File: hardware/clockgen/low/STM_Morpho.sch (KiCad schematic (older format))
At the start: 13 parts, among them CN10 Conn_02x19_Odd_Even, CN7 Conn_02x19_Odd_Even, J1 Conn_02x20_Odd_Even, U1 74ALVC164245DLG4, U2 74ALVC164245DLG4

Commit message: Two PCBs are routed
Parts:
- J1: symbol Connector_Generic:Conn_02x20_Counter_Clockwise -> Connector_Generic:Conn_02x20_Odd_Even
- U1, U2: symbol 2021-08-26_08-32-07:74ALVC164245DLG4 -> STM_Morpho-rescue:74ALVC164245DLG4-2021-08-26_08-32-07
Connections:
- net +3V3: now also J1.3 (Pin_3); no longer J1.2 (Pin_2)
- net GND: now also J1.2 (Pin_2), J1.38 (Pin_38), J1.4 (Pin_4); no longer J1.21 (Pin_21), J1.22 (Pin_22), J1.39 (Pin_39)
- net NC: now also J1.37 (Pin_37), J1.39 (Pin_39); no longer J1.19 (Pin_19), J1.20 (Pin_20)
- net PA0_5V: now also J1.27 (Pin_27); no longer J1.7 (Pin_7)
- net PA10_5V: now also J1.35 (Pin_35); no longer J1.3 (Pin_3)
- net PA11_5V: now also J1.34 (Pin_34); no longer J1.24 (Pin_24)
- net PA12_5V: now also J1.32 (Pin_32); no longer J1.25 (Pin_25)
- net PA13_5V: now also J1.30 (Pin_30); no longer J1.26 (Pin_26)
- net PA14_5V: now also J1.28 (Pin_28); no longer J1.27 (Pin_27)
- net PA15_5V: now also J1.26 (Pin_26); no longer J1.28 (Pin_28)
- net PA1_5V: now also J1.15 (Pin_15); no longer J1.13 (Pin_13)
- net PA2_5V: now also J1.13 (Pin_13); no longer J1.14 (Pin_14)
- net PA3_5V: now also J1.11 (Pin_11); no longer J1.15 (Pin_15)
- net PA4_5V: now also J1.9 (Pin_9); no longer J1.16 (Pin_16)
- net PA5_5V: now also J1.7 (Pin_7); no longer J1.17 (Pin_17)
- net PA6_5V: now also J1.19 (Pin_19); no longer J1.11 (Pin_11)
- net PA7_5V: now also J1.17 (Pin_17); no longer J1.12 (Pin_12)
- net PA8_5V: now also J1.5 (Pin_5); no longer J1.18 (Pin_18)
- net PA9_5V: now also J1.36 (Pin_36); no longer J1.23 (Pin_23)
- net PB10_5V: now also J1.33 (Pin_33); no longer J1.4 (Pin_4)
- net PB5_5V: now also J1.31 (Pin_31); no longer J1.5 (Pin_5)
- net PB6_5V: now also J1.29 (Pin_29); no longer J1.6 (Pin_6)
- net PB8_5V: now also J1.23 (Pin_23); no longer J1.9 (Pin_9)
- net PB9_5V: now also J1.21 (Pin_21); no longer J1.10 (Pin_10)
- net PC0_5V: now also J1.24 (Pin_24); no longer J1.29 (Pin_29)
- net PC10_5V: now also J1.6 (Pin_6); no longer J1.38 (Pin_38)
- net PC1_5V: now also J1.22 (Pin_22); no longer J1.30 (Pin_30)
- net PC2_5V: now also J1.20 (Pin_20); no longer J1.31 (Pin_31)
- net PC3_5V: now also J1.18 (Pin_18); no longer J1.32 (Pin_32)
- net PC4_5V: now also J1.16 (Pin_16); no longer J1.33 (Pin_33)
- net PC5_5V: now also J1.14 (Pin_14); no longer J1.34 (Pin_34)
- net PC6_5V: now also J1.12 (Pin_12); no longer J1.35 (Pin_35)
- net PC7_5V: now also J1.25 (Pin_25); no longer J1.8 (Pin_8)
- net PC8_5V: now also J1.10 (Pin_10); no longer J1.36 (Pin_36)
- net PC9_5V: now also J1.8 (Pin_8); no longer J1.37 (Pin_37)
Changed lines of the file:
@@
 PA3
 $Comp
-L 2021-08-26_08-32-07:74ALVC164245DLG4 U1
+L STM_Morpho-rescue:74ALVC164245DLG4-2021-08-26_08-32-07 U1
 U 1 1 6128B1C2
 P 4400 1050
@@
 PULLUP
 $Comp
-L 2021-08-26_08-32-07:74ALVC164245DLG4 U2
+L STM_Morpho-rescue:74ALVC164245DLG4-2021-08-26_08-32-07 U2
 U 1 1 6130056B
 P 8750 1050
@@
 Text Label 13300 2600 0    50   ~ 0
 PA9_5V
-Text Label 12800 2600 2    50   ~ 0
-PA8_5V
-Text Label 12800 2500 2    50   ~ 0
-PA5_5V
-Text Label 12800 2400 2    50   ~ 0
-PA4_5V
-Text Label 12800 2300 2    50   ~ 0
-PA3_5V
-Text Label 12800 2200 2    50   ~ 0
-PA2_5V
-Text Label 12800 2100 2    50   ~ 0
-PA1_5V
-$Comp
-L Connector_Generic:Conn_02x20_Counter_Clockwise J1
-U 1 1 612BBAFC
-P 13000 1800
-F 0 "J1" H 13050 2917 50  0000 C CNN
-F 1 "Conn_02x20_Odd_Even" H 13050 2826 50  0000 C CNN
-F 2 "Connector_PinHeader_2.54mm:PinHeader_2x20_P2.54mm_Vertical" H 13000 1800 50  0001 C CNN
-F 3 "~" H 13000 1800 50  0001 C CNN
-	1    13000 1800
-	1    0    0    -1
-$EndComp
 $Comp
 L power:GND #PWR06
@@
 	1    0    0    -1
 $EndComp
-Text Label 12800 2000 2    50   ~ 0
-PA7_5V
-Text Label 12800 1900 2    50   ~ 0
-PA6_5V
-Text Label 12800 1800 2    50   ~ 0
-PB9_5V
-Text Label 12800 1700 2    50   ~ 0
-PB8_5V
-Text Label 12800 1600 2    50   ~ 0
-PC7_5V
-Text Label 12800 1500 2    50   ~ 0
-PA0_5V
-Text Label 12800 1400 2    50   ~ 0
-PB6_5V
-Text Label 12800 1300 2    50   ~ 0
-PB5_5V
-Text Label 12800 1200 2    50   ~ 0
-PB10_5V
-Text Label 12800 1100 2    50   ~ 0
-PA10_5V
 Text Label 14400 2850 2    50   ~ 0
 PULLUP
+$Comp
+L Connector_Generic:Conn_02x20_Odd_Even J1
+U 1 1 612BBAFC
+P 13000 1800
+F 0 "J1" H 13050 2917 50  0000 C CNN
+F 1 "Conn_02x20_Odd_Even" H 13050 2826 50  0000 C CNN
+F 2 "Connector_PinHeader_2.54mm:PinHeader_2x20_P2.54mm_Vertical" H 13000 1800 50  0001 C CNN
+F 3 "~" H 13000 1800 50  0001 C CNN
+	1    13000 1800
+	1    0    0    -1
+$EndComp
+Connection ~ 14400 2550
+Text Label 12800 2600 2    50   ~ 0
+PA10_5V
+Text Label 12800 2500 2    50   ~ 0
+PB10_5V
+Text Label 12800 2400 2    50   ~ 0
+PB5_5V
+Text Label 12800 2300 2    50   ~ 0
+PB6_5V
+Text Label 12800 2200 2    50   ~ 0
+PA0_5V
+Text Label 12800 2100 2    50   ~ 0
+PC7_5V
+Text Label 12800 2000 2    50   ~ 0
+PB8_5V
+Text Label 12800 1900 2    50   ~ 0
+PB9_5V
+Text Label 12800 1800 2    50   ~ 0
+PA6_5V
+Text Label 12800 1700 2    50   ~ 0
+PA7_5V
+Text Label 12800 1600 2    50   ~ 0
+PA1_5V
+Text Label 12800 1500 2    50   ~ 0
+PA2_5V
+Text Label 12800 1400 2    50   ~ 0
+PA3_5V
+Text Label 12800 1300 2    50   ~ 0
+PA4_5V
+Text Label 12800 1200 2    50   ~ 0
+PA5_5V
+Text Label 12800 1100 2    50   ~ 0
+PA8_5V
 $EndSCHEMATC

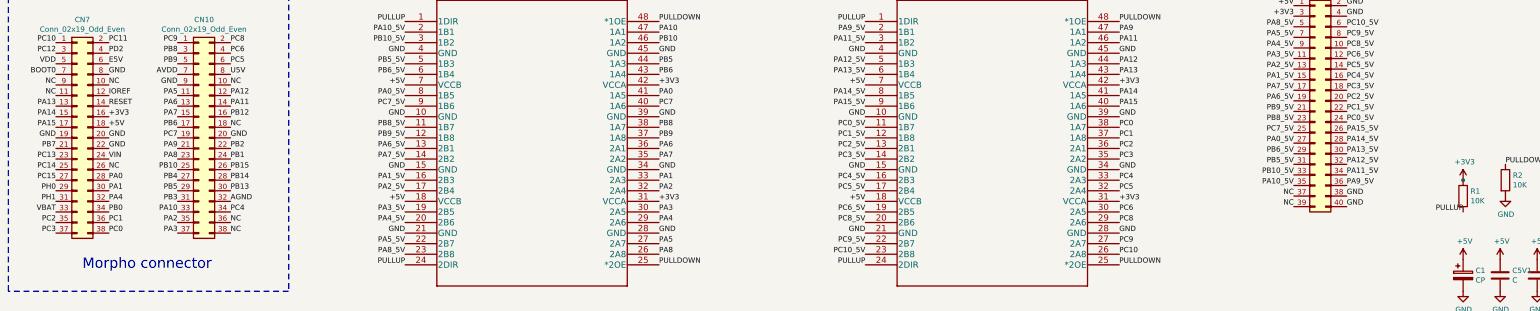
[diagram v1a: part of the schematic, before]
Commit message: Screw terminal adapter added
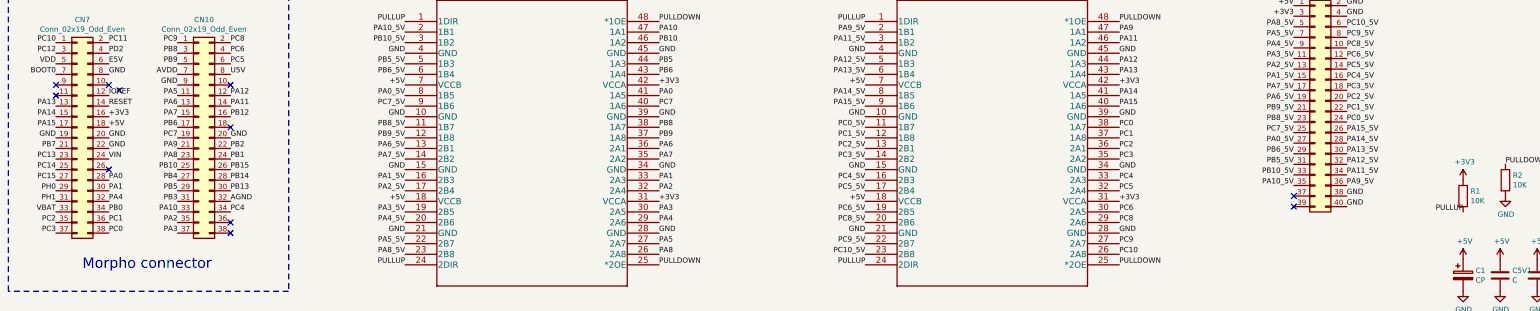
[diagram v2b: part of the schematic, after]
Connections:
- removed net NC: CN10.10 (Pin_10), CN10.18 (Pin_18), CN10.36 (Pin_36), CN10.38 (Pin_38), CN7.10 (Pin_10), CN7.11 (Pin_11), CN7.26 (Pin_26), CN7.9 (Pin_9), J1.37 (Pin_37), J1.39 (Pin_39)
- no-connect marks 0 -> 11
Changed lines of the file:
@@
 $EndDescr
-$Comp
-L Connector_Generic:Conn_02x19_Odd_Even CN7
-U 1 1 5F9F2DD0
-P 1300 2150
-F 0 "CN7" H 1350 3267 50  0000 C CNN
-F 1 "Conn_02x19_Odd_Even" H 1350 3176 50  0000 C CNN
-F 2 "Connector_PinSocket_2.54mm:PinSocket_2x19_P2.54mm_Vertical" H 1300 2150 50  0001 C CNN
-F 3 "~" H 1300 2150 50  0001 C CNN
-	1    1300 2150
-	1    0    0    -1
-$EndComp
 $Comp
 L Connector_Generic:Conn_02x19_Odd_Even CN10
@@
 Text Label 1100 1550 2    50   ~ 0
 BOOT0
-Text Label 1100 1650 2    50   ~ 0
-NC
-Text Label 1100 1750 2    50   ~ 0
-NC
 Text Label 1100 1850 2    50   ~ 0
 PA13
@@
 Text Label 1600 1550 0    50   ~ 0
 GND
-Text Label 1600 1650 0    50   ~ 0
-NC
 Text Label 1600 1750 0    50   ~ 0
 IOREF
@@
 Text Label 1600 2350 0    50   ~ 0
 VIN
-Text Label 1600 2450 0    50   ~ 0
-NC
 Text Label 1600 2550 0    50   ~ 0
 PA0
@@
 Text Label 2750 1550 0    50   ~ 0
 U5V
-Text Label 2750 1650 0    50   ~ 0
-NC
 Text Label 2750 1750 0    50   ~ 0
 PA12
@@
 Text Label 2750 1950 0    50   ~ 0
 PB12
-Text Label 2750 2050 0    50   ~ 0
-NC
 Text Label 2750 2150 0    50   ~ 0
 GND
@@
 Text Label 2750 2850 0    50   ~ 0
 PC4
-Text Label 2750 2950 0    50   ~ 0
-NC
-Text Label 2750 3050 0    50   ~ 0
-NC
 Text Label 2250 1250 2    50   ~ 0
 PC9
@@
 Text Label 15300 7750 1    50   ~ 0
 GND
-Text Label 12800 2800 2    50   ~ 0
-NC
-Text Label 12800 2700 2    50   ~ 0
-NC
 Text Label 13300 2800 0    50   ~ 0
 GND
@@
 	1    0    0    -1
 $EndComp
-Connection ~ 14400 2550
 Text Label 12800 2600 2    50   ~ 0
 PA10_5V
@@
 Text Label 12800 1100 2    50   ~ 0
 PA8_5V
+NoConn ~ 12800 2800
+NoConn ~ 12800 2700
+NoConn ~ 2750 2950
+NoConn ~ 2750 3050
+$Comp
+L Connector_Generic:Conn_02x19_Odd_Even CN7
+U 1 1 5F9F2DD0
+P 1300 2150
+F 0 "CN7" H 1350 3267 50  0000 C CNN
+F 1 "Conn_02x19_Odd_Even" H 1350 3176 50  0000 C CNN
+F 2 "Connector_PinSocket_2.54mm:PinSocket_2x19_P2.54mm_Vertical" H 1300 2150 50  0001 C CNN
+F 3 "~" H 1300 2150 50  0001 C CNN
+	1    1300 2150
+	1    0    0    -1
+$EndComp
+NoConn ~ 1600 2450
+NoConn ~ 1100 1650
+NoConn ~ 1100 1750
+NoConn ~ 2750 1650
+NoConn ~ 2750 2050
+NoConn ~ 1600 1650
+NoConn ~ 1700 1700
 $EndSCHEMATC
